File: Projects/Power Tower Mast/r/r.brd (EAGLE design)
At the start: 15.9 x 20.9 mm, 29 parts

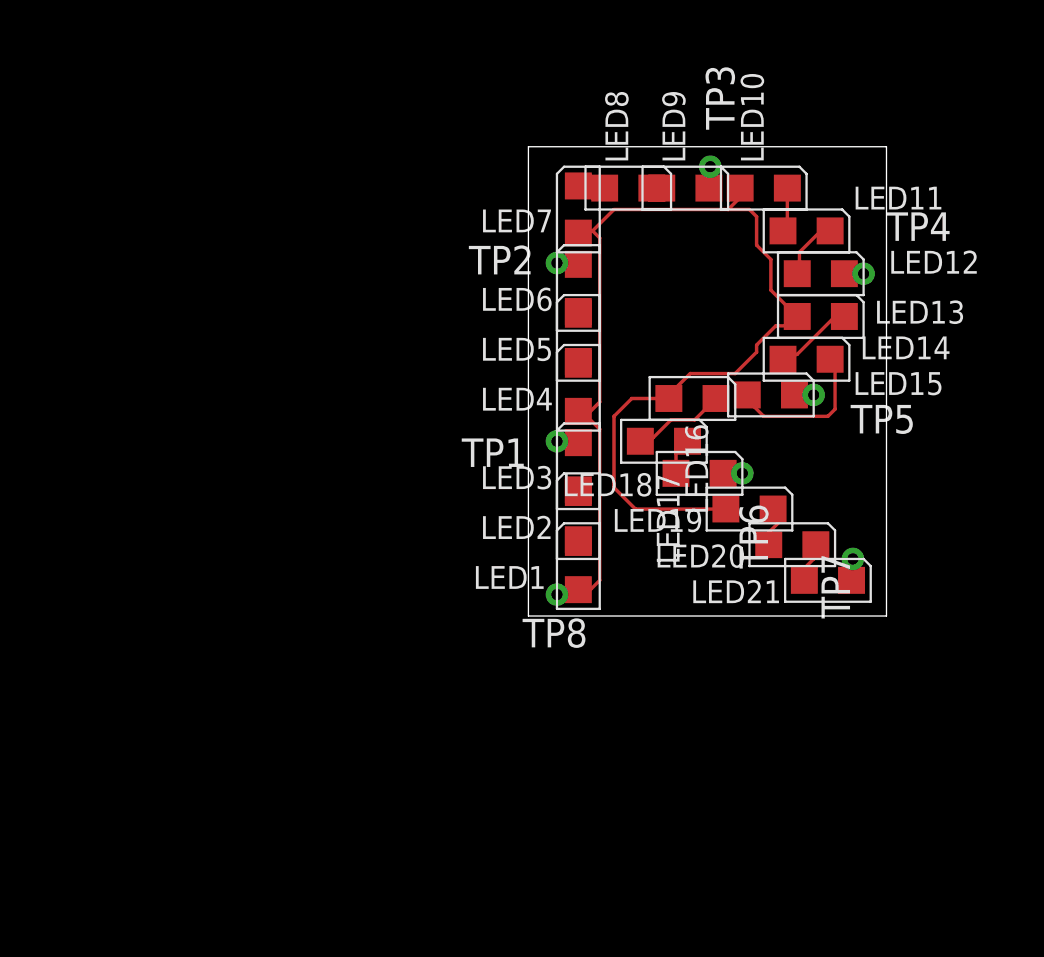
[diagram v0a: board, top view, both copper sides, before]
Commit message: updated with extra vias and panelized
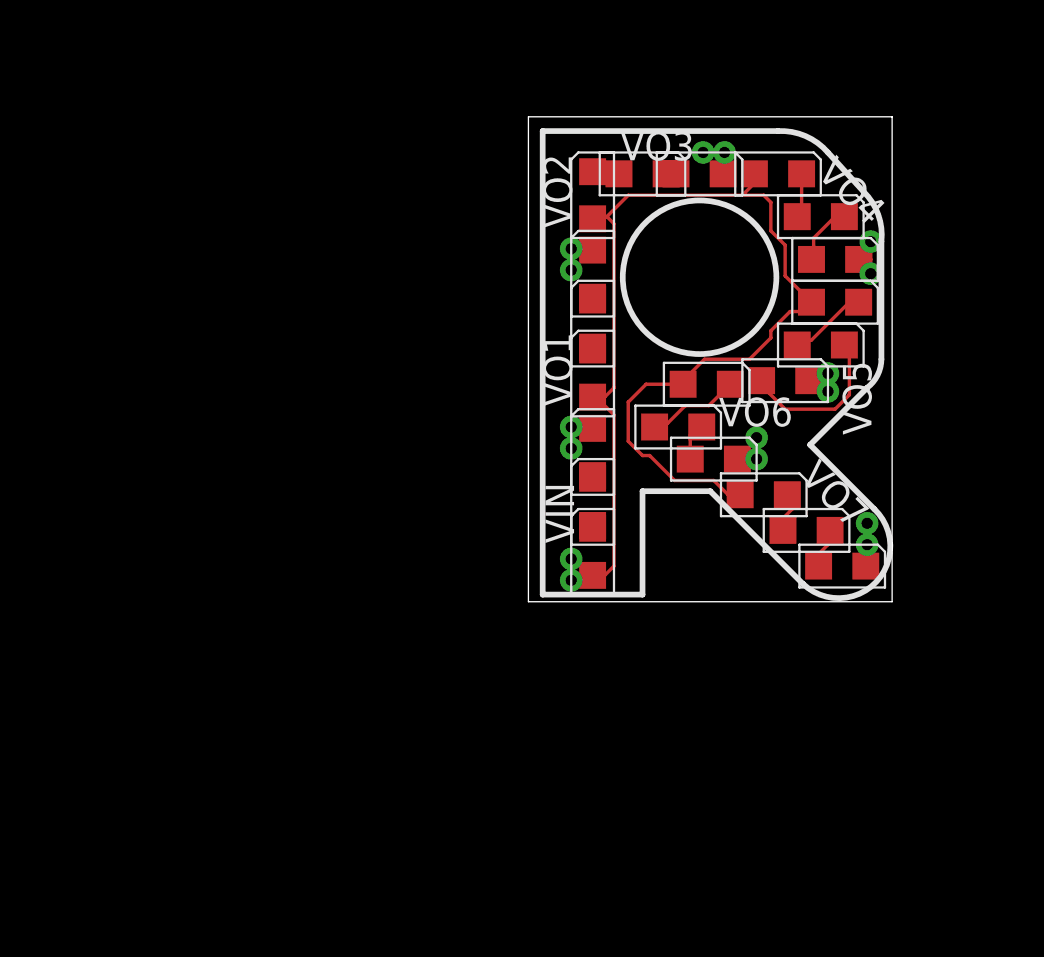
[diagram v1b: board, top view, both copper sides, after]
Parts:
- removed TP1, TP2, TP3, TP4, TP5, TP6, TP7, TP8: (no value), CyberRailGuru:P1-20
- added VIN, VIN1, VO1, VO10, VO11, VO12, VO13, VO14, VO2, VO3, VO4, VO5, VO6, VO7, VO8, VO9: (no value), CyberRailGuru:P1-20
- moved LED10 0.90 mm to (11.1, 19.1)
- moved LED13 0.90 mm to (13.7, 13.3)
- moved LED7 0.90 mm to (2.86, 18.1)
- moved LED8 0.90 mm to (5.08, 19.1)
- moved LED9 0.90 mm to (7.62, 19.1)
- moved LED17 0.90 mm to (6.67, 7.78)
- moved LED18 0.90 mm to (8.26, 6.35)
- moved LED3 0.90 mm to (2.86, 6.67)
- moved LED1 0.90 mm to (2.86, 2.22)
- moved LED2 0.90 mm to (2.86, 4.45)
- moved LED12 0.90 mm to (13.7, 15.2)
- moved LED14 0.90 mm to (13.0, 11.4)
- moved LED15 0.90 mm to (11.4, 9.84)
- moved LED16 0.90 mm to (7.94, 9.68)
- moved LED19 0.90 mm to (10.5, 4.76)
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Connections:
- removed net VIN5: LED1.A, LED10.A, LED13.A, LED16.A, LED19.A, LED4.A, LED7.A, TP8.TP
- removed net VOUT26: LED3.C, TP1.TP
- removed net VOUT27: LED6.C, TP2.TP
- removed net VOUT28: LED9.C, TP3.TP
- removed net VOUT29: LED12.C, TP4.TP
- removed net VOUT30: LED15.C, TP5.TP
- removed net VOUT31: LED18.C, TP6.TP
- removed net VOUT32: LED21.C, TP7.TP
- new net VIN: LED1.A, LED10.A, LED13.A, LED16.A, LED19.A, LED4.A, LED7.A, VIN.TP, VIN1.TP
- new net VOUT1: LED3.C, VO1.TP, VO8.TP
- new net VOUT2: LED6.C, VO2.TP, VO9.TP
- new net VOUT3: LED9.C, VO10.TP, VO3.TP
- new net VOUT4: LED12.C, VO11.TP, VO4.TP
- new net VOUT5: LED15.C, VO12.TP, VO5.TP
- new net VOUT6: LED18.C, VO13.TP, VO6.TP
- new net VOUT7: LED21.C, VO14.TP, VO7.TP
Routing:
- net VIN: track 0.00 -> 53.2 mm
- net VIN5: track 53.1 -> 0.00 mm
- net VOUT2: track 0.00 -> 1.97 mm
- net VOUT4: track 0.00 -> 1.97 mm
- net VOUT3: track 0.00 -> 1.97 mm
- net VOUT1: track 0.00 -> 1.97 mm
- net VOUT7: track 0.00 -> 1.91 mm
- net VOUT6: track 0.00 -> 1.81 mm
- net VOUT5: track 0.00 -> 1.71 mm
- net VOUT27: track 1.01 -> 0.00 mm
- net VOUT26: track 1.01 -> 0.00 mm
- net VOUT28: track 1.01 -> 0.00 mm
- net VOUT32: track 0.96 -> 0.00 mm
- net VOUT31: track 0.86 -> 0.00 mm
- net VOUT30: track 0.85 -> 0.00 mm
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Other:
- board size 15.9 x 20.9 mm -> 16.2 x 21.6 mm

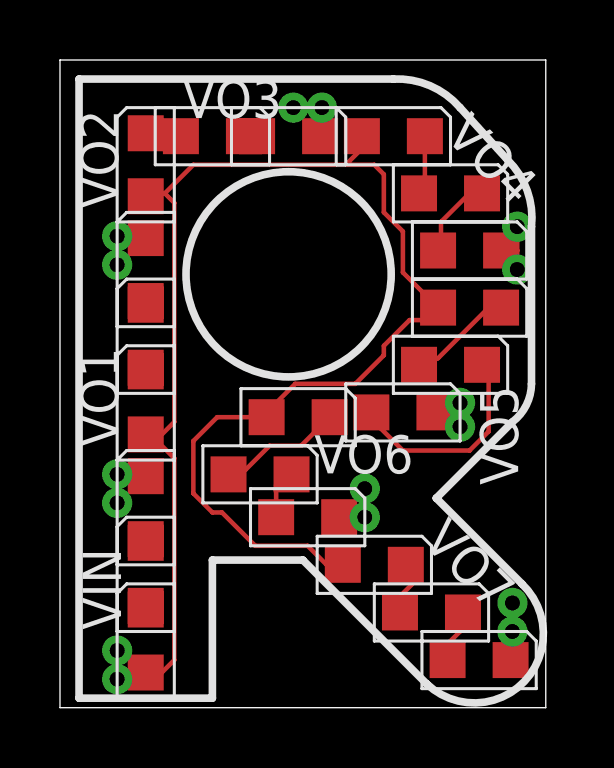
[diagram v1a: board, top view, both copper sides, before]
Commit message: reworking some letters
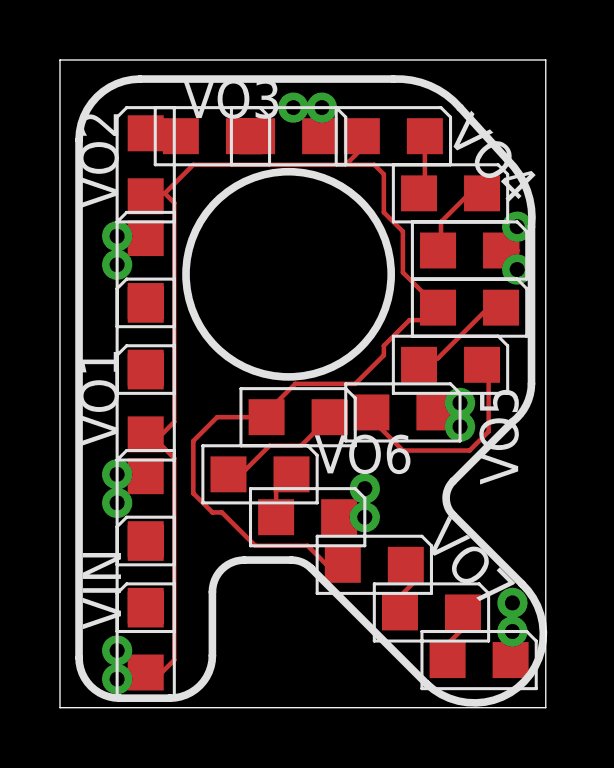
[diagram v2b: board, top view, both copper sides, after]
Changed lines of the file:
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@@
 <wire x1="0" y1="21.59" x2="0" y2="0" width="0" layer="20"/>
 <text x="0.635" y="0.635" size="20.32" layer="201" font="fixed" ratio="22" distance="27">R</text>
-<wire x1="0.635" y1="0.3175" x2="0.635" y2="20.955" width="0.254" layer="21"/>
-<wire x1="0.635" y1="20.955" x2="11.1125" y2="20.955" width="0.254" layer="21"/>
-<wire x1="0.635" y1="0.3175" x2="5.08" y2="0.3175" width="0.254" layer="21"/>
-<wire x1="5.08" y1="0.3175" x2="5.08" y2="4.92125" width="0.254" layer="21"/>
-<wire x1="5.08" y1="4.92125" x2="8.09625" y2="4.92125" width="0.254" layer="21"/>
-<wire x1="8.09625" y1="4.92125" x2="12.22375" y2="0.79375" width="0.254" layer="21"/>
-<wire x1="15.39875" y1="4.1275" x2="12.54125" y2="6.985" width="0.254" layer="21"/>
+<wire x1="0.635" y1="18.922009375" x2="0.635" y2="1.6645375" width="0.254" layer="21"/>
+<wire x1="0.635" y1="1.6645375" x2="1.9820375" y2="0.3175" width="0.254" layer="21" curve="90"/>
+<wire x1="1.9820375" y1="0.3175" x2="3.660096875" y2="0.3175" width="0.254" layer="21"/>
+<wire x1="0.635" y1="18.922009375" x2="2.667990625" y2="20.955" width="0.254" layer="21" curve="-90"/>
+<wire x1="2.667990625" y1="20.955" x2="11.1125" y2="20.955" width="0.254" layer="21"/>
+<wire x1="3.660096875" y1="0.3175" x2="5.08" y2="1.737403125" width="0.254" layer="21" curve="90"/>
+<wire x1="5.08" y1="1.737403125" x2="5.08" y2="3.856325" width="0.254" layer="21"/>
+<wire x1="5.08" y1="3.856325" x2="6.144925" y2="4.92125" width="0.254" layer="21" curve="-90"/>
+<wire x1="6.144925" y1="4.92125" x2="7.712828125" y2="4.92125" width="0.254" layer="21"/>
+<wire x1="7.712828125" y1="4.92125" x2="8.36736875" y2="4.65013125" width="0.254" layer="21" curve="-44.999863"/>
+<wire x1="8.36736875" y1="4.65013125" x2="12.22375" y2="0.79375" width="0.254" layer="21"/>
+<wire x1="15.39875" y1="4.1275" x2="13.102515625" y2="6.423734375" width="0.254" layer="21"/>
+<wire x1="13.102515625" y1="6.423734375" x2="13.102515625" y2="7.546265625" width="0.254" layer="21" curve="-90"/>
+<wire x1="13.102515625" y1="7.546265625" x2="15.08125" y2="9.525" width="0.254" layer="21"/>
 <wire x1="12.22375" y1="0.79375" x2="15.39875" y2="4.1275" width="0.254" layer="21" curve="180"/>
 <wire x1="11.1125" y1="20.955" x2="13.335" y2="20.0025" width="0.254" layer="21" curve="-51.842773"/>
 <wire x1="14.9225" y1="18.25625" x2="15.71625" y2="16.03375" width="0.254" layer="21" curve="-51.842773"/>
 <wire x1="15.71625" y1="10.795" x2="15.08125" y2="9.525" width="0.254" layer="21" curve="-51.842773"/>
-<wire x1="12.54125" y1="6.985" x2="15.08125" y2="9.525" width="0.254" layer="21"/>
 <wire x1="15.71625" y1="10.795" x2="15.71625" y2="16.03375" width="0.254" layer="21"/>
 <wire x1="14.9225" y1="18.25625" x2="13.335" y2="20.0025" width="0.254" layer="21"/>

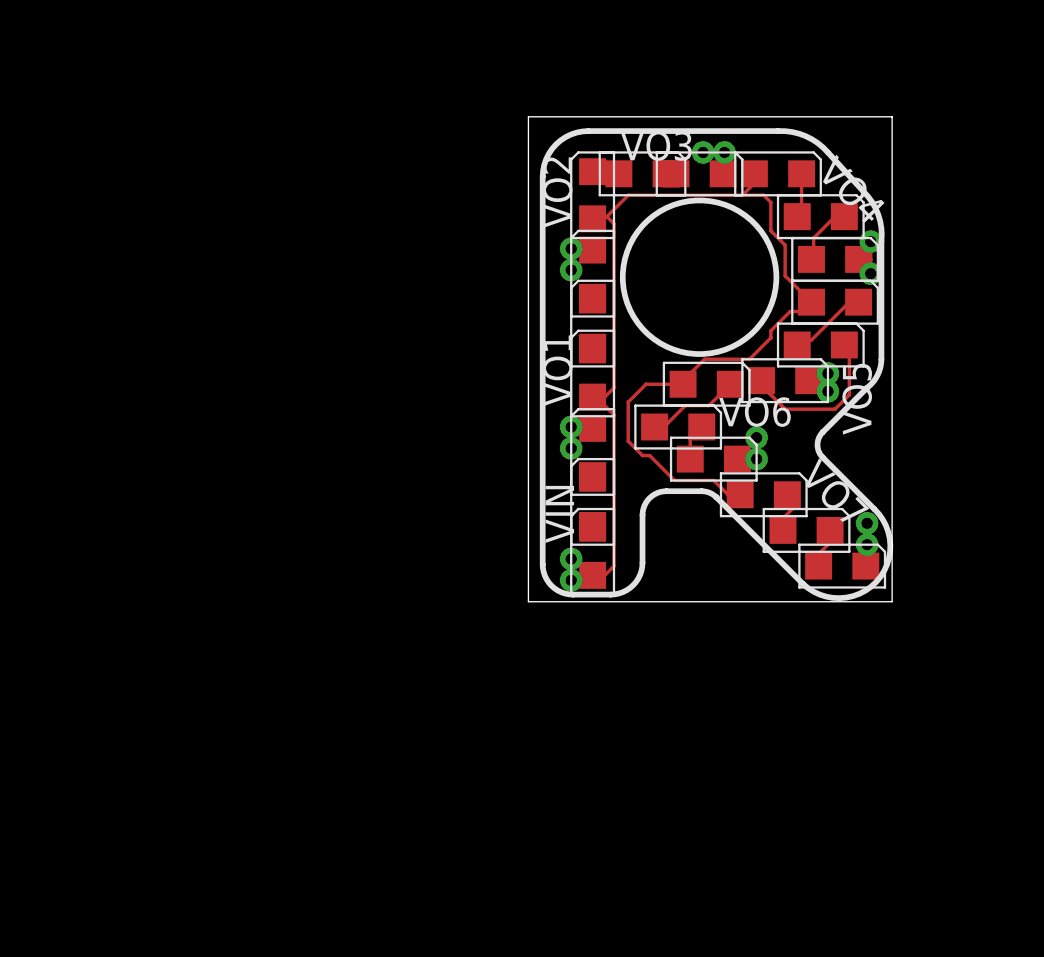
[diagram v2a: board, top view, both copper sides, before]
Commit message: fixed ratio for all letters; continued to update layouts
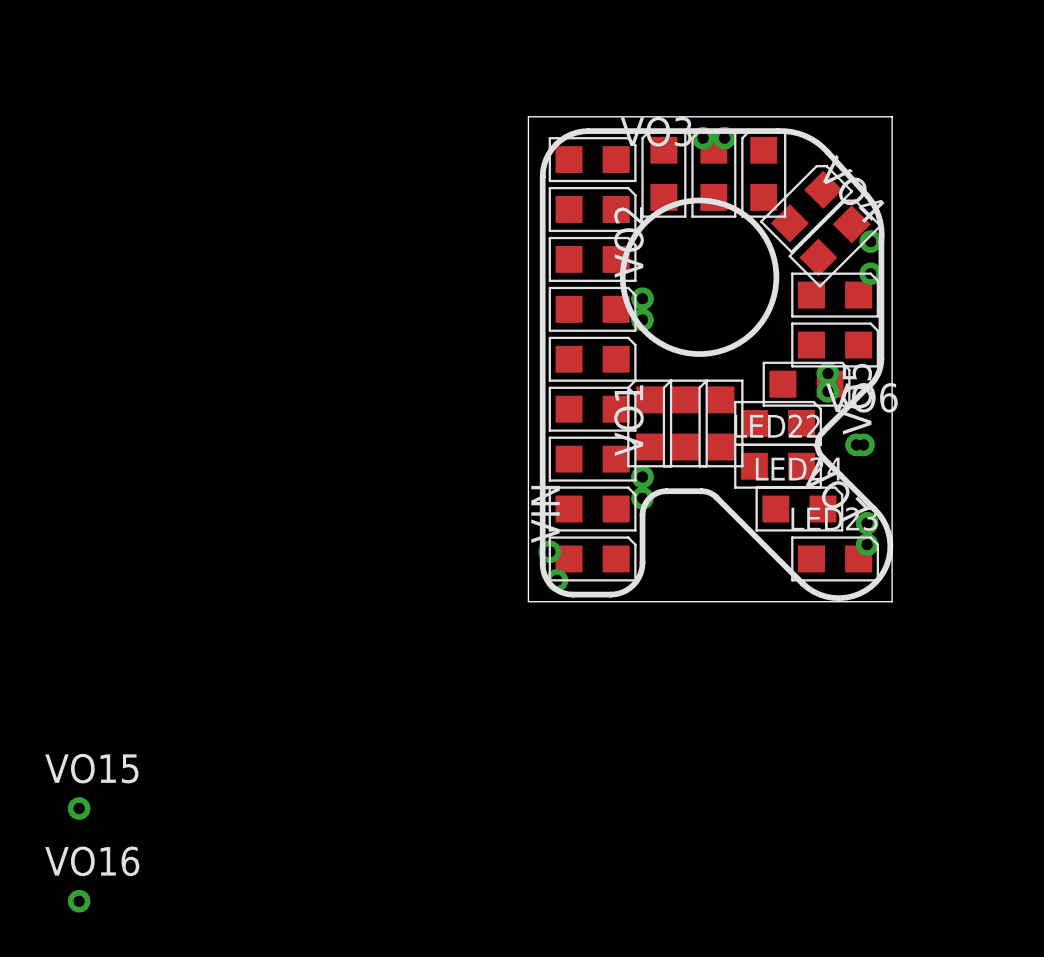
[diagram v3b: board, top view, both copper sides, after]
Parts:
- added LED22, LED23, LED24: (no value), CyberRailGuru:LED_0805
- added VO15, VO16: (no value), CyberRailGuru:P1-20
- moved LED21 10.7 mm to (5.40, 7.94), turned to 0 degrees
- moved LED20 7.20 mm to (6.99, 7.94), turned to 0 degrees
- moved LED17 6.02 mm to (12.4, 9.68)
- moved LED16 5.98 mm to (13.7, 11.4)
- moved LED11 5.13 mm to (8.26, 19.1), turned to 0 degrees
- moved LED10 5.08 mm to (6.03, 19.1), turned to 0 degrees
- moved LED12 4.96 mm to (10.5, 19.1), turned to 0 degrees
- moved LED9 4.80 mm to (2.86, 19.7)
- moved VO6 4.80 mm to (14.9, 6.99)
- moved LED14 4.67 mm to (13.7, 16.1), turned to 315 degrees
- moved VO13 4.46 mm to (14.6, 6.99)
- moved LED13 4.44 mm to (12.4, 17.6), turned to 315 degrees
- moved LED15 4.41 mm to (13.7, 13.7)
- moved VO1 3.88 mm to (5.08, 5.56)
- moved VO2 3.88 mm to (5.08, 13.5)
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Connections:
- new net N$1: LED23.C, LED24.A
- new net N$2: LED22.C, LED23.A
- new net N$3: LED24.C, VO15.TP, VO16.TP
- net VIN: now also LED22.A
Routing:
- net VIN: track 53.2 -> 0.00 mm
- net N$59: track 7.09 -> 0.00 mm
- net N$62: track 4.11 -> 0.00 mm
- net N$60: track 3.47 -> 0.00 mm
- net N$57: track 2.75 -> 0.00 mm
- net N$63: track 2.22 -> 0.00 mm
- net N$64: track 2.10 -> 0.00 mm
- net N$58: track 1.99 -> 0.00 mm
- net VOUT2: track 1.97 -> 0.00 mm
- net VOUT4: track 1.97 -> 0.00 mm
- net VOUT3: track 1.97 -> 0.00 mm
- net VOUT1: track 1.97 -> 0.00 mm
- net VOUT7: track 1.91 -> 0.00 mm
- net VOUT6: track 1.81 -> 0.00 mm
- net VOUT5: track 1.71 -> 0.00 mm
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
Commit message: final updates before fab.  added new letters for future projects.
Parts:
- moved VO16 37.2 mm to (13.5, 2.86)
- moved VO15 32.0 mm to (5.87, 9.68)
- moved VO7 12.4 mm to (4.92, 9.68)
- moved VO11 11.4 mm to (4.29, 17.8)
- moved VO12 11.0 mm to (11.1, 20.2)
- moved VO10 10.1 mm to (4.29, 11.1)
- moved VO8 8.42 mm to (13.5, 4.45)
- moved VO13 7.15 mm to (14.9, 14.1)
- moved VO4 7.05 mm to (9.53, 20.2)
- moved VO9 6.20 mm to (3.65, 6.51)
- moved VO3 4.58 mm to (4.29, 19.5)
- moved VO14 3.84 mm to (13.5, 6.99)
- moved VO5 2.86 mm to (14.9, 12.5)
- moved VO6 1.72 mm to (13.5, 7.94)
- moved VO1 1.56 mm to (3.65, 4.92)
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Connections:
- removed net N$3: LED24.C, VO15.TP, VO16.TP
- new net VOUT8: LED24.C, VO16.TP, VO8.TP
- net VOUT1: now also VO9.TP; no longer VO8.TP
- net VOUT2: now also VO10.TP; no longer VO9.TP
- net VOUT3: now also VO11.TP; no longer VO10.TP
- net VOUT4: now also VO12.TP; no longer VO11.TP
- net VOUT5: now also VO13.TP; no longer VO12.TP
- net VOUT6: now also VO14.TP; no longer VO13.TP
- net VOUT7: now also VO15.TP; no longer VO14.TP
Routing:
- net VIN: track 0.00 -> 51.1 mm, vias 0 -> 6
- net N$1: track 0.00 -> 6.09 mm, vias 0 -> 2
- net N$61: track 0.00 -> 5.64 mm, vias 0 -> 2
- net N$62: track 0.00 -> 4.44 mm
- net N$2: track 0.00 -> 4.24 mm
- net N$59: track 0.00 -> 3.50 mm
- net N$60: track 0.00 -> 3.36 mm
- net N$51: track 0.00 -> 3.23 mm
- net N$57: track 0.00 -> 3.18 mm
- net N$58: track 0.00 -> 3.18 mm
- net N$56: track 0.00 -> 3.09 mm
- net N$55: track 0.00 -> 2.99 mm
- net N$54: track 0.00 -> 2.95 mm
- net N$53: track 0.00 -> 2.95 mm
- net N$52: track 0.00 -> 2.95 mm
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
